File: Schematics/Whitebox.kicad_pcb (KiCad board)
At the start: 2 copper layers, 105 parts, among them J1 AudioJack3_SwitchTR, J2 AudioJack3_SwitchTR, J3 Barrel_Jack, J4 AudioJack3_SwitchTR, J5 Conn_01x06, Q1 2N7002, Q2 2N7002, Q3 2N7002, Q4 2N7002, Q5 2N7002, Q6 2N7002, Q7 2N7002, Q8 2N7002, SW1 SW_Push, SW2 Rotary_Encoder_Switch, SW3 Rotary_Encoder_Switch, SW4 Rotary_Encoder_Switch, SW5 Rotary_Encoder_Switch, SW6 SW_Push, SW7 SW_Push, SW8 SW_Push, SW9 SW_Push, U1 TLV320AIC3106IRGZR, U2 MCP16311MS, U3 LP2985-3.3, U4 LP2985-1.8, U5 PocketBeagle, U6 ATmega328P-AU, U7 NHD-24064CZ-FSW-GBW, U8 PCA9306, U9 TCA6416APWR, Y1 Crystal_GND24_Small

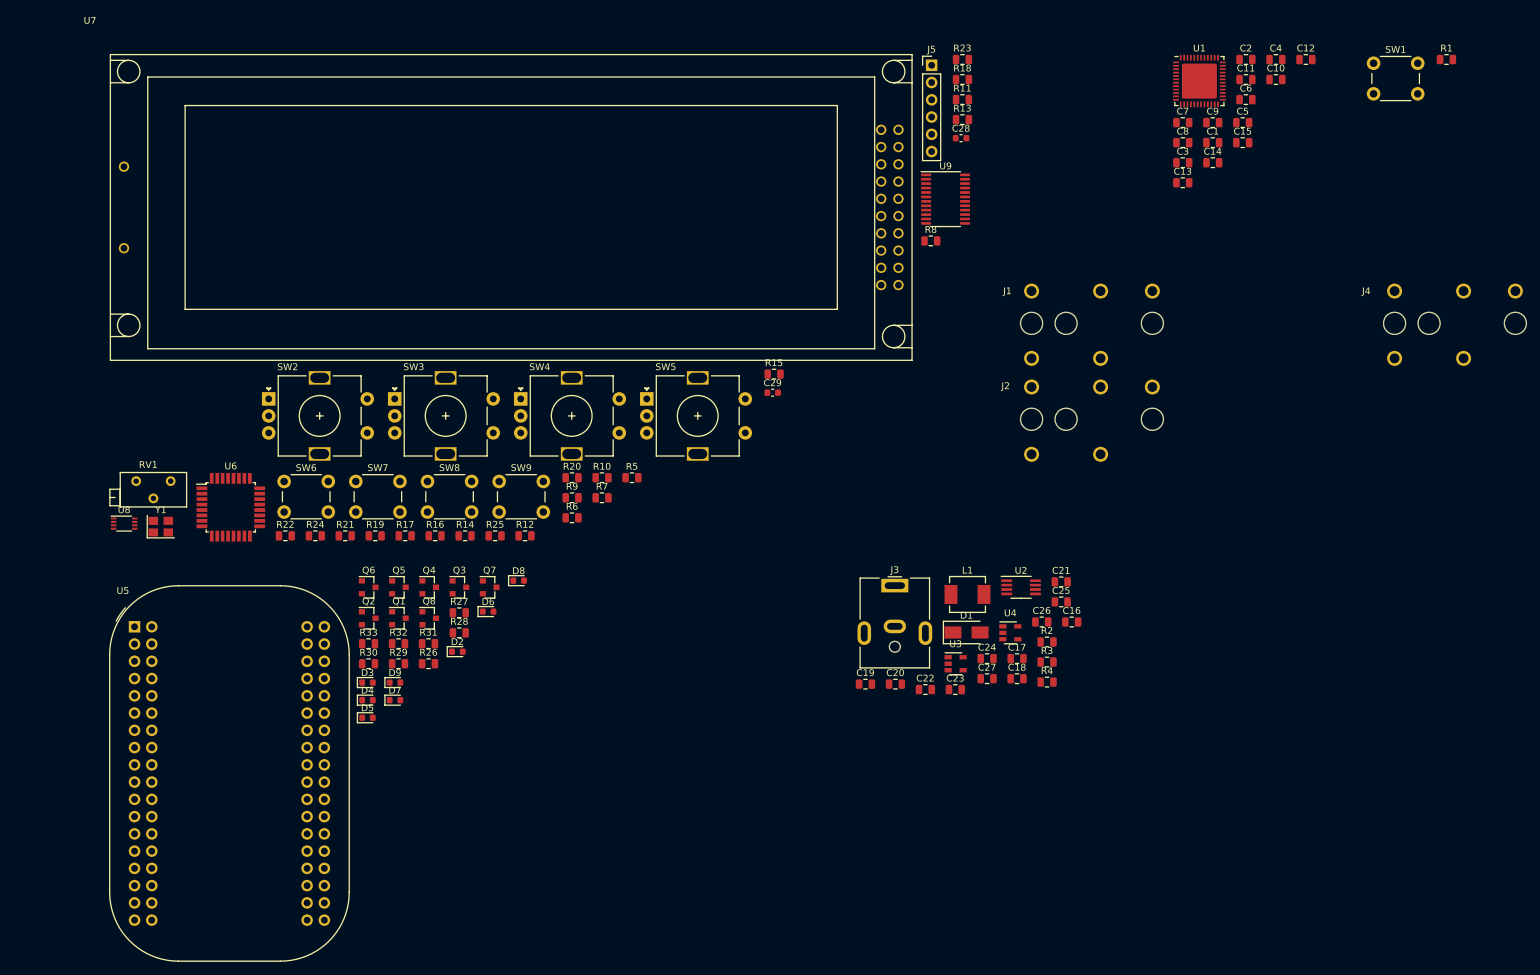
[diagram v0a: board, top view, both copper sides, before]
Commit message: Finished initial component placement
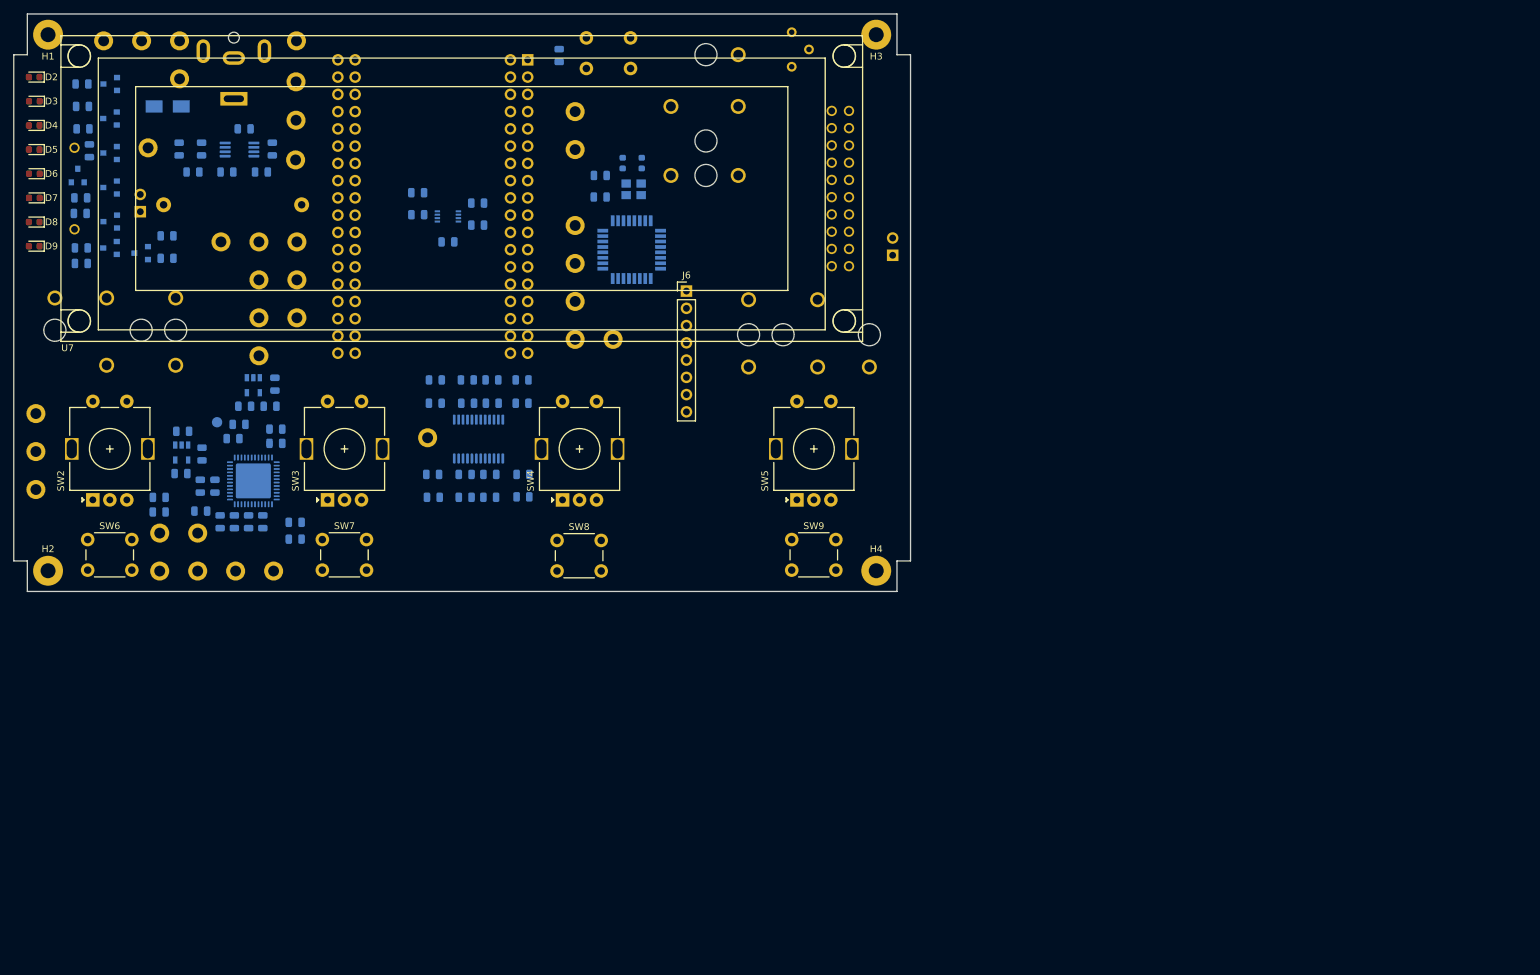
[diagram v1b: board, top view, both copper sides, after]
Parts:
- added C30: 1uF, Capacitor_SMD:C_0805_2012Metric, B.Cu at (131.3, 48.8)
- added C31: 0.1uF, Capacitor_SMD:C_0805_2012Metric, B.Cu at (131.3, 51.9)
- added H1: MountingHole_Pad, MountingHole:MountingHole_2.2mm_M2_Pad, F.Cu at (50.0, 28.0)
- added H2: MountingHole_Pad, MountingHole:MountingHole_2.2mm_M2_Pad, F.Cu at (50.0, 107.0)
- added H3: MountingHole_Pad, MountingHole:MountingHole_2.2mm_M2_Pad, F.Cu at (172.0, 28.0)
- added H4: MountingHole_Pad, MountingHole:MountingHole_2.2mm_M2_Pad, F.Cu at (172.0, 107.0)
- added J6: Conn_01x08, Connector_PinHeader_2.54mm:PinHeader_1x08_P2.54mm_Vertical, F.Cu at (144.0, 65.8)
- added J7: Conn_01x02, Connector_PinHeader_2.54mm:PinHeader_1x02_P2.54mm_Vertical, B.Cu at (63.6, 54.1)
- added P1: star_ground, Whitebox:star_ground, B.Cu at (74.9, 85.1)
- added TP1: TestPoint, TestPoint:TestPoint_Keystone_5010-5014_Multipurpose, B.Cu at (127.6, 39.4)
- added TP10: TestPoint, TestPoint:TestPoint_Keystone_5010-5014_Multipurpose, B.Cu at (86.7, 64.1)
- added TP11: TestPoint, TestPoint:TestPoint_Keystone_5010-5014_Multipurpose, B.Cu at (86.7, 58.5)
- added TP12: TestPoint, TestPoint:TestPoint_Keystone_5010-5014_Multipurpose, B.Cu at (66.5, 101.4)
- added TP13: TestPoint, TestPoint:TestPoint_Keystone_5010-5014_Multipurpose, B.Cu at (72.1, 101.4)
- added TP14: TestPoint, TestPoint:TestPoint_Keystone_5010-5014_Multipurpose, B.Cu at (86.6, 29.0)
- added TP15: TestPoint, TestPoint:TestPoint_Keystone_5010-5014_Multipurpose, B.Cu at (69.4, 34.5)
- added TP16: TestPoint, TestPoint:TestPoint_Keystone_5010-5014_Multipurpose, B.Cu at (86.5, 46.5)
- added TP17: TestPoint, TestPoint:TestPoint_Keystone_5010-5014_Multipurpose, B.Cu at (81.1, 58.5)
- added TP18: TestPoint, TestPoint:TestPoint_Keystone_5010-5014_Multipurpose, B.Cu at (105.9, 87.4)
- added TP19: TestPoint, TestPoint:TestPoint_Keystone_5010-5014_Multipurpose, B.Cu at (64.8, 44.7)
- added TP2: TestPoint, TestPoint:TestPoint_Keystone_5010-5014_Multipurpose, B.Cu at (127.6, 67.3)
- added TP20: TestPoint, TestPoint:TestPoint_Keystone_5010-5014_Multipurpose, B.Cu at (75.5, 58.5)
- added TP21: TestPoint, TestPoint:TestPoint_Keystone_5010-5014_Multipurpose, B.Cu at (72.1, 107.0)
- added TP22: TestPoint, TestPoint:TestPoint_Keystone_5010-5014_Multipurpose, B.Cu at (81.1, 75.3)
- added TP23: TestPoint, TestPoint:TestPoint_Keystone_5010-5014_Multipurpose, B.Cu at (58.2, 29.0)
- added TP24: TestPoint, TestPoint:TestPoint_Keystone_5010-5014_Multipurpose, B.Cu at (63.8, 29.0)
- added TP25: TestPoint, TestPoint:TestPoint_Keystone_5010-5014_Multipurpose, B.Cu at (69.4, 29.0)
- added TP26: TestPoint, TestPoint:TestPoint_Keystone_5010-5014_Multipurpose, B.Cu at (127.6, 45.0)
- added TP27: TestPoint, TestPoint:TestPoint_Keystone_5010-5014_Multipurpose, B.Cu at (127.6, 61.7)
- added TP28: TestPoint, TestPoint:TestPoint_Keystone_5010-5014_Multipurpose, B.Cu at (127.6, 56.1)
- added TP29: TestPoint, TestPoint:TestPoint_Keystone_5010-5014_Multipurpose, B.Cu at (133.2, 72.9)
- added TP3: TestPoint, TestPoint:TestPoint_Keystone_5010-5014_Multipurpose, B.Cu at (127.6, 72.9)
- added TP30: TestPoint, TestPoint:TestPoint_Keystone_5010-5014_Multipurpose, B.Cu at (86.6, 35.0)
- added TP31: TestPoint, TestPoint:TestPoint_Keystone_5010-5014_Multipurpose, B.Cu at (86.6, 40.6)
- added TP32: TestPoint, TestPoint:TestPoint_Keystone_5010-5014_Multipurpose, B.Cu at (48.3, 89.4)
- added TP33: TestPoint, TestPoint:TestPoint_Keystone_5010-5014_Multipurpose, B.Cu at (48.3, 95.0)
- added TP34: TestPoint, TestPoint:TestPoint_Keystone_5010-5014_Multipurpose, B.Cu at (48.3, 83.8)
- added TP35: TestPoint, TestPoint:TestPoint_Keystone_5010-5014_Multipurpose, B.Cu at (66.5, 107.0)
- added TP4: TestPoint, TestPoint:TestPoint_Keystone_5010-5014_Multipurpose, B.Cu at (83.2, 107.0)
- added TP5: TestPoint, TestPoint:TestPoint_Keystone_5010-5014_Multipurpose, B.Cu at (77.7, 107.0)
- added TP6: TestPoint, TestPoint:TestPoint_Keystone_5010-5014_Multipurpose, B.Cu at (81.1, 69.7)
- added TP8: TestPoint, TestPoint:TestPoint_Keystone_5010-5014_Multipurpose, B.Cu at (86.7, 69.7)
- added TP9: TestPoint, TestPoint:TestPoint_Keystone_5010-5014_Multipurpose, B.Cu at (81.1, 64.1)
- C1, C10, C11, C12, C13, C14, C15, C16, C17, C18, C19, C2, C20, C21, C22, C23, C24, C25, C26, C27, C28, C29, C3, C4, C5, C6, C7, C8, C9, D1, J1, J2, J3, J4, Q1, Q2, Q3, Q4, Q5, Q6, Q7, Q8, R1, R10, R11, R12, R13, R14, R15, R16, R17, R18, R19, R2, R20, R21, R22, R23, R24, R25, R26, R27, R28, R29, R3, R30, R31, R32, R33, R4, R5, R6, R7, R8, R9, RV1, SW1, U1, U2, U3, U4, U5, U6, U8, U9, Y1: moved to B.Cu
- J5: value Conn_01x06 -> Conn_01x02; footprint Connector_PinHeader_2.54mm:PinHeader_1x06_P2.54mm_Vertical -> Connector_PinHeader_2.54mm:PinHeader_1x02_P2.54mm_Vertical; moved to B.Cu
- L1: footprint Inductor_SMD:L_Vishay_IHLP-2020 -> Inductor_THT:L_Axial_L16.0mm_D6.3mm_P20.32mm_Horizontal_Fastron_VHBCC; moved to B.Cu
- moved C15 168.5 mm to (66.4, 98.3)
- moved C4 165.8 mm to (79.6, 99.7), turned to 90 degrees
- moved C2 165.6 mm to (75.4, 99.7), turned to 90 degrees
- moved C11 165.1 mm to (72.5, 94.5), turned to 270 degrees
- moved C14 162.7 mm to (66.4, 96.1)
- moved C10 162.3 mm to (77.3, 87.5), turned to 180 degrees
- moved C12 161.1 mm to (83.6, 86.1), turned to 180 degrees
- moved C1 158.5 mm to (72.5, 98.2)
- moved C9 156.3 mm to (74.6, 94.5), turned to 270 degrees
- moved C6 153.2 mm to (86.4, 99.8), turned to 180 degrees
- moved C5 152.4 mm to (86.4, 102.3), turned to 180 degrees
- moved U1 151.2 mm to (80.3, 93.7), turned to 180 degrees
- moved C3 149.3 mm to (77.5, 99.7), turned to 90 degrees
- moved C7 147.6 mm to (81.7, 99.7), turned to 90 degrees
- moved C16 145.8 mm to (72.6, 44.9), turned to 270 degrees
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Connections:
- C1 pad 1: GND -> GNDA
- C11 pad 1: GND -> GNDA
- C2 pad 1: GND -> GNDA
- C20 pad 1: +5V -> Net-(C20-Pad1)
- C21 pad 1: +5V -> Net-(C20-Pad1)
- C24 pad 2: GND -> GNDA
- C26 pad 2: GND -> GNDA
- C3 pad 1: GND -> GNDA
- C4 pad 1: GND -> GNDA
- C7 pad 1: GND -> GNDA
- C9 pad 1: GND -> GNDA
- J1 pad S: GND -> GNDA
- J2 pad S: GND -> GNDA
- J5 pad 1: +5V -> Net-(J5-Pad1)
- J5 pad 2: GND -> +5V
- L1 pad 2: +5V -> Net-(C20-Pad1)
- R2 pad 2: +5V -> Net-(C20-Pad1)
- R8 pad 1: +5V -> +3V3
- R9 pad 1: +5V -> +3V3
- U1 pad 15: GND -> GNDA
- U1 pad 20: GND -> GNDA
- U1 pad 21: GND -> GNDA
- U1 pad 26: GND -> GNDA
- U1 pad 45: Net-(U1-Pad45) -> GND
- U1 pad 46: Net-(U1-Pad46) -> GND
- U1 pad 49: GND -> GNDA
- U3 pad 2: GND -> GNDA
- U5 pad 38: Net-(U5-Pad38) -> /Processor/LED0
- U5 pad 40: Net-(U5-Pad40) -> /Processor/LED1
- U5 pad 42: Net-(U5-Pad42) -> /Processor/LED2
- U5 pad 44: Net-(U5-Pad44) -> /Processor/LED3
- U5 pad 46: Net-(U5-Pad46) -> /Processor/LED4
- U5 pad 53: Net-(U5-Pad53) -> /Processor/LED5
- U5 pad 54: Net-(U5-Pad54) -> /Processor/LED6
- U5 pad 55: Net-(U5-Pad55) -> /Processor/LED7
- U5 pad 62: /~POCKETBEAGLE_RESET -> /~AIC_RESET
- U7 pad 20: +5V -> Net-(J5-Pad1)
- U9 pad 10: /ExternalIO/ENC3_A -> /ExternalIO/ENC1_A
- U9 pad 11: /ExternalIO/ENC3_B -> /ExternalIO/ENC1_B
- U9 pad 15: /ExternalIO/ENC2_SW -> /ExternalIO/IO_SW0
- U9 pad 16: /ExternalIO/ENC3_SW -> /ExternalIO/IO_SW1
- U9 pad 17: /ExternalIO/IO_SW0 -> /ExternalIO/IO_SW2
- U9 pad 18: /ExternalIO/IO_SW1 -> /ExternalIO/IO_SW3
- U9 pad 19: /ExternalIO/IO_SW2 -> /ExternalIO/ENC2_SW
- U9 pad 20: /ExternalIO/IO_SW3 -> /ExternalIO/ENC3_SW
- U9 pad 4: /ExternalIO/ENC0_A -> /ExternalIO/ENC2_A
- U9 pad 5: /ExternalIO/ENC0_B -> /ExternalIO/ENC2_B
- U9 pad 6: /ExternalIO/ENC1_A -> /ExternalIO/ENC3_A
- U9 pad 7: /ExternalIO/ENC1_B -> /ExternalIO/ENC3_B
- U9 pad 8: /ExternalIO/ENC2_A -> /ExternalIO/ENC0_A
- U9 pad 9: /ExternalIO/ENC2_B -> /ExternalIO/ENC0_B
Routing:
- added copper zone on In1.Cu, net GND
- added copper zone on In1.Cu, net GNDA
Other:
- board outline added: 132 x 85 mm
- copper layers 2 -> 4
- board text added: "+5V"
- board text added: "1V8"
- board text added: "3V3A"
- board text added: "GND"
